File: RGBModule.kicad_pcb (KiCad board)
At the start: 2 copper layers, 17.8 x 24.4 mm, 9 parts, among them P1 CONN_01X04

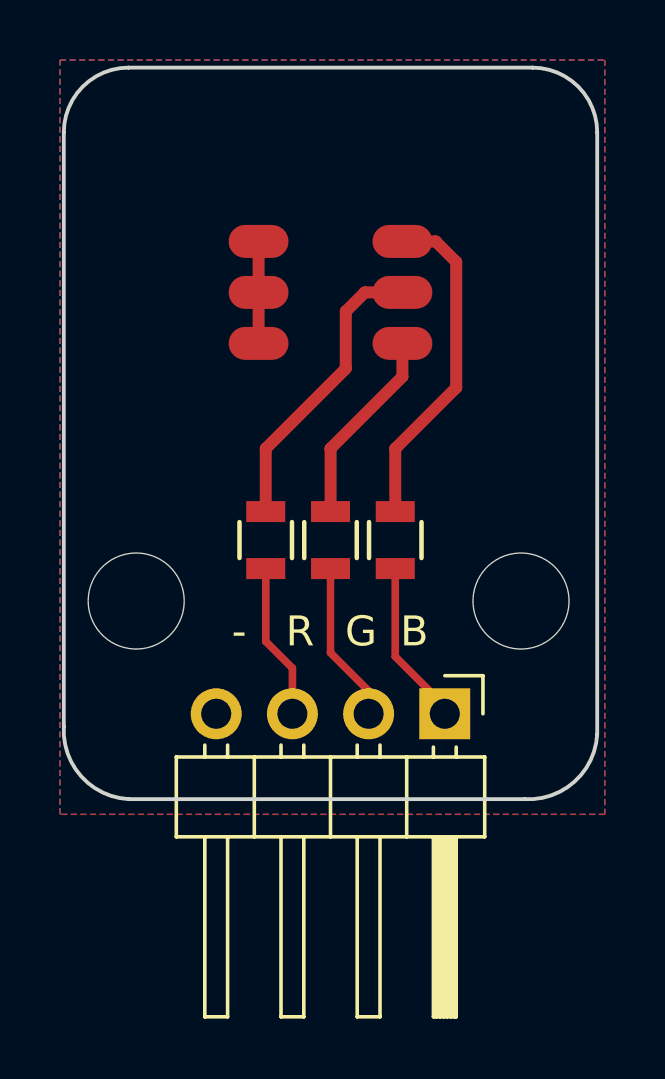
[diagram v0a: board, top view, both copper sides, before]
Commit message: Problema con los colores cambiados
El verde estaba como B y el azul como G, ya está corregido
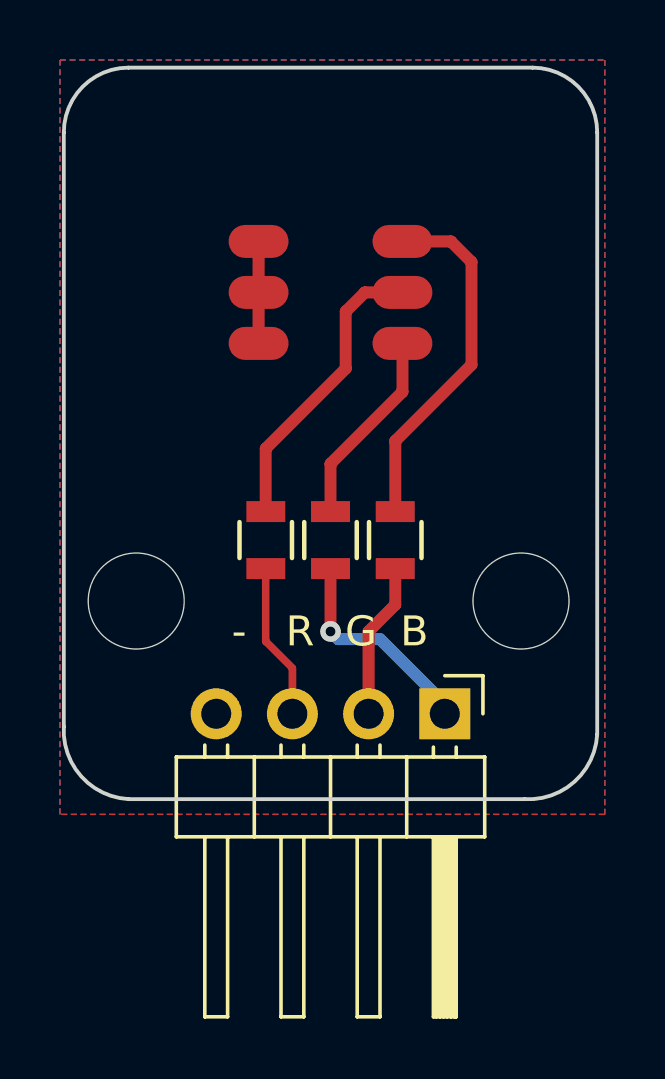
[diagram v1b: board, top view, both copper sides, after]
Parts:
- LED1: footprint SparkFun-LED:LED-TRICOLOR-5050 -> lib_fp:LED-TRICOLOR-5050
- P1: footprint Pin_Headers:Pin_Header_Angled_1x04_Pitch2.54mm -> lib_fp:Pin_Header_Angled_1x04_Pitch2.54mm
- R1, R2, R3: footprint Resistors_SMD:R_0805 -> lib_fp:R_0805
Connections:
- R1 pad 1: BLUE -> GREEN
- R2 pad 2: GREEN -> BLUE
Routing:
- net BLUE: track 5.53 -> 7.67 mm, vias 0 -> 1
- net Net-(LED1-Pad3): track 11.2 -> 12.0 mm
